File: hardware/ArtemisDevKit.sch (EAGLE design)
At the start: 77 parts, among them J1 USB, J10 SMD, J11 SMD, J12 PTH, J14 PTH, J2 CORTEX_JTAG_DEBUG_MINIMUM_PTH, J22 PTH, J23 PTH, J24 PTH, J25 PTH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

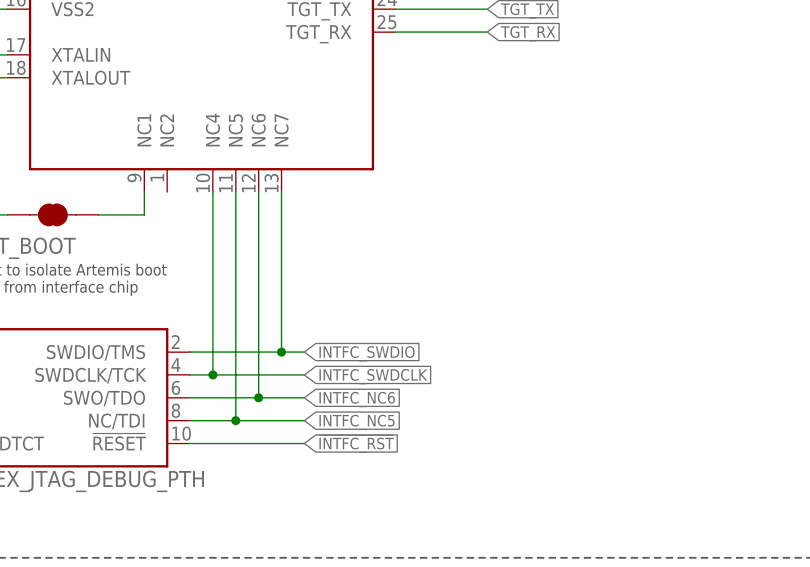
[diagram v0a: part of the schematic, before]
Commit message: add test points for interface JTAG
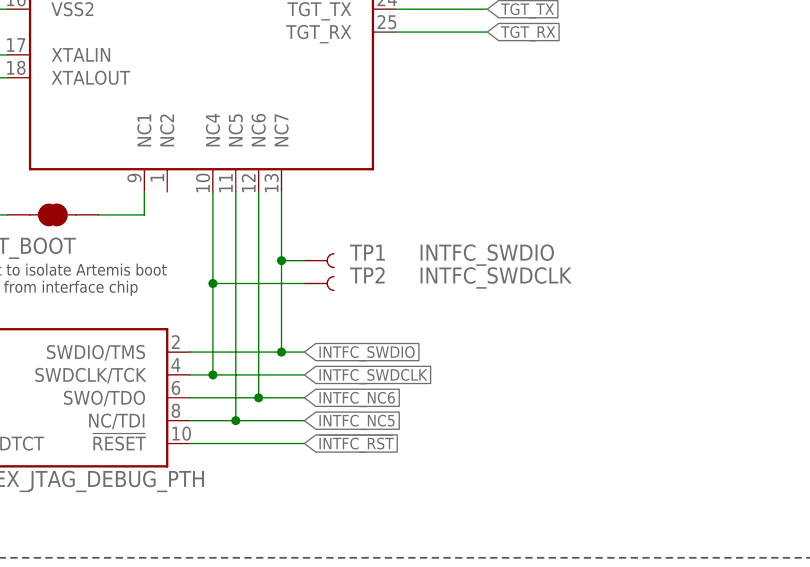
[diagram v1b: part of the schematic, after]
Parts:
- added TP1: INTFC_SWDIO, SparkFun-Connectors:TEST-POINT3
- added TP2: INTFC_SWDCLK, SparkFun-Connectors:TEST-POINT3
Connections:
- net INTFC_SWDCLK: now also TP2.1
- net INTFC_SWDIO: now also TP1.1
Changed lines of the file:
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@@
 <part name="U1" library="SparkFun-IC-Microcontroller" deviceset="DAPLINK_KL26Z128VFM4" device=""/>
 <part name="LOGO2" library="SparkFun-Aesthetics" deviceset="SFE_LOGO_NAME_FLAME" device=".2_INCH"/>
+<part name="TP1" library="SparkFun-Connectors" deviceset="TEST-POINT" device="3" value="INTFC_SWDIO"/>
+<part name="TP2" library="SparkFun-Connectors" deviceset="TEST-POINT" device="3" value="INTFC_SWDCLK"/>
 </parts>
 <sheets>
@@
 <instance part="U1" gate="G$1" x="88.9" y="187.96" smashed="yes"/>
 <instance part="LOGO2" gate="G$1" x="337.82" y="241.3" smashed="yes"/>
+<instance part="TP1" gate="G$1" x="101.6" y="144.78" smashed="yes">
+<attribute name="NAME" x="106.68" y="144.78" size="1.778" layer="95" font="vector"/>
+<attribute name="VALUE" x="114.3" y="144.78" size="1.778" layer="96" font="vector"/>
+</instance>
+<instance part="TP2" gate="G$1" x="101.6" y="142.24" smashed="yes">
+<attribute name="NAME" x="106.68" y="142.24" size="1.778" layer="95" font="vector"/>
+<attribute name="VALUE" x="114.3" y="142.24" size="1.778" layer="96" font="vector"/>
+</instance>
 </instances>
 <busses>
@@
 <label x="101.6" y="134.62" size="1.27" layer="95" font="vector" xref="yes"/>
 <wire x1="99.06" y1="134.62" x2="88.9" y2="134.62" width="0.1524" layer="91"/>
-<wire x1="99.06" y1="134.62" x2="99.06" y2="152.4" width="0.1524" layer="91"/>
+<wire x1="99.06" y1="134.62" x2="99.06" y2="144.78" width="0.1524" layer="91"/>
 <junction x="99.06" y="134.62"/>
 <pinref part="U1" gate="G$1" pin="NC7"/>
+<pinref part="TP1" gate="G$1" pin="1"/>
+<wire x1="99.06" y1="144.78" x2="99.06" y2="152.4" width="0.1524" layer="91"/>
+<wire x1="101.6" y1="144.78" x2="99.06" y2="144.78" width="0.1524" layer="91"/>
+<junction x="99.06" y="144.78"/>
 </segment>
 </net>
@@
 <label x="101.6" y="132.08" size="1.27" layer="95" font="vector" xref="yes"/>
 <wire x1="91.44" y1="132.08" x2="88.9" y2="132.08" width="0.1524" layer="91"/>
-<wire x1="91.44" y1="132.08" x2="91.44" y2="152.4" width="0.1524" layer="91"/>
+<wire x1="91.44" y1="132.08" x2="91.44" y2="142.24" width="0.1524" layer="91"/>
 <junction x="91.44" y="132.08"/>
 <pinref part="U1" gate="G$1" pin="NC4"/>
-</segment>
-</net>
+<pinref part="TP2" gate="G$1" pin="1"/>
+<wire x1="91.44" y1="142.24" x2="91.44" y2="152.4" width="0.1524" layer="91"/>
+<wire x1="101.6" y1="142.24" x2="91.44" y2="142.24" width="0.1524" layer="91"/>
+<junction x="91.44" y="142.24"/>
+</segment>
+</net>

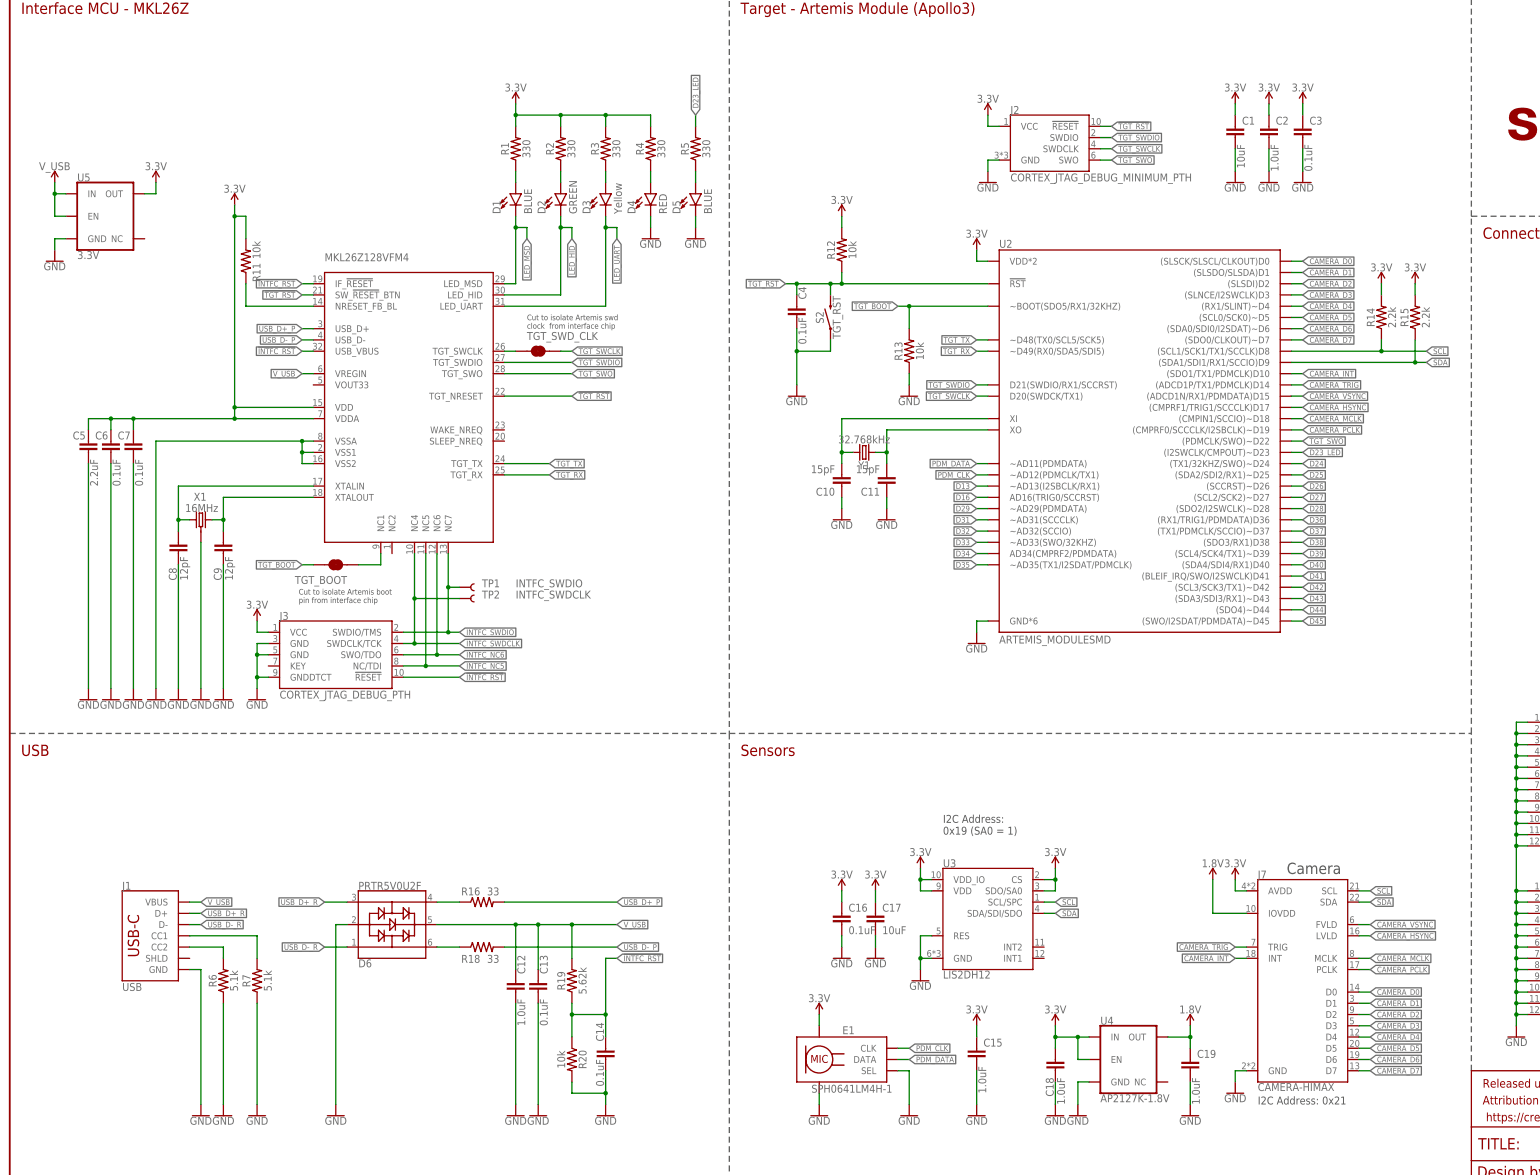
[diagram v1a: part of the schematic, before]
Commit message: fix camera connector
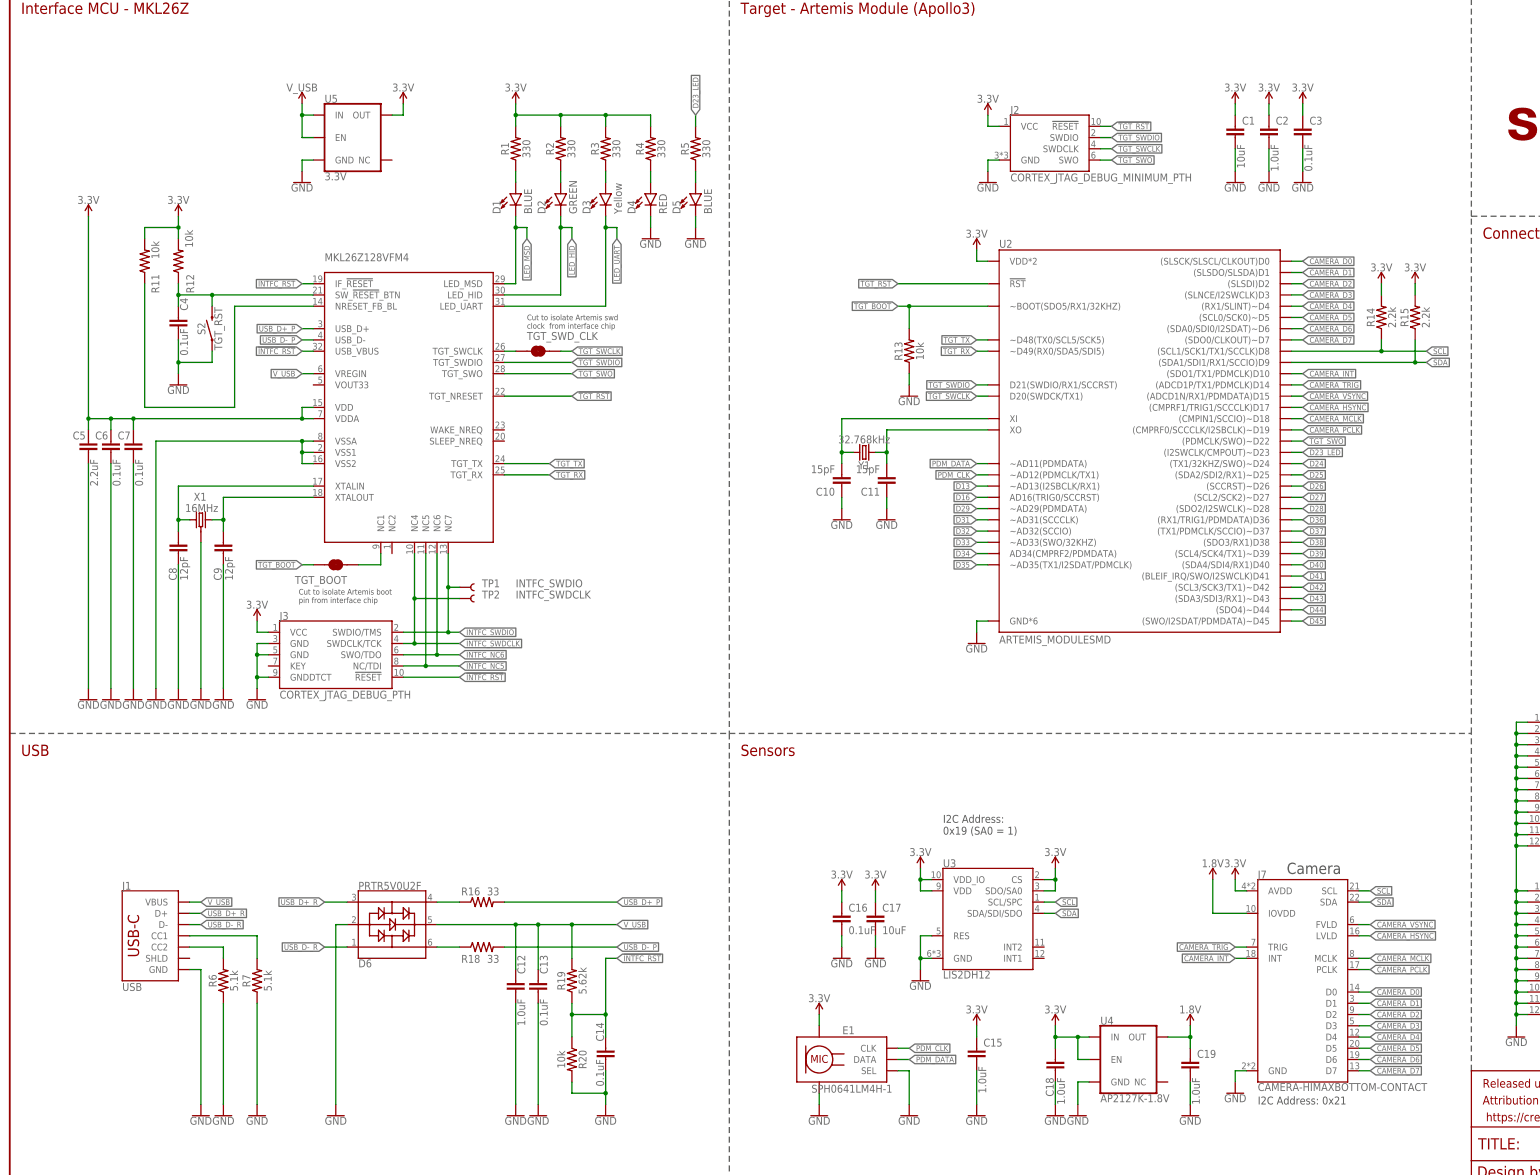
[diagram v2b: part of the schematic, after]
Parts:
- J7: value CAMERA-HIMAX -> CAMERA-HIMAXBOTTOM-CONTACT; device SparkFun-Connectors:CAMERA-HIMAX -> SparkFun-Connectors:CAMERA-HIMAXBOTTOM-CONTACT
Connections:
- new net !RST!_BTN: C4.1, R12.1, S2.2, U1.SW_!RESET!_BTN
- net !TGT_RST: no longer C4.1, R12.1, S2.2, U1.SW_!RESET!_BTN
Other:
- moved on the sheet: C4, R11, R12, S2, U5

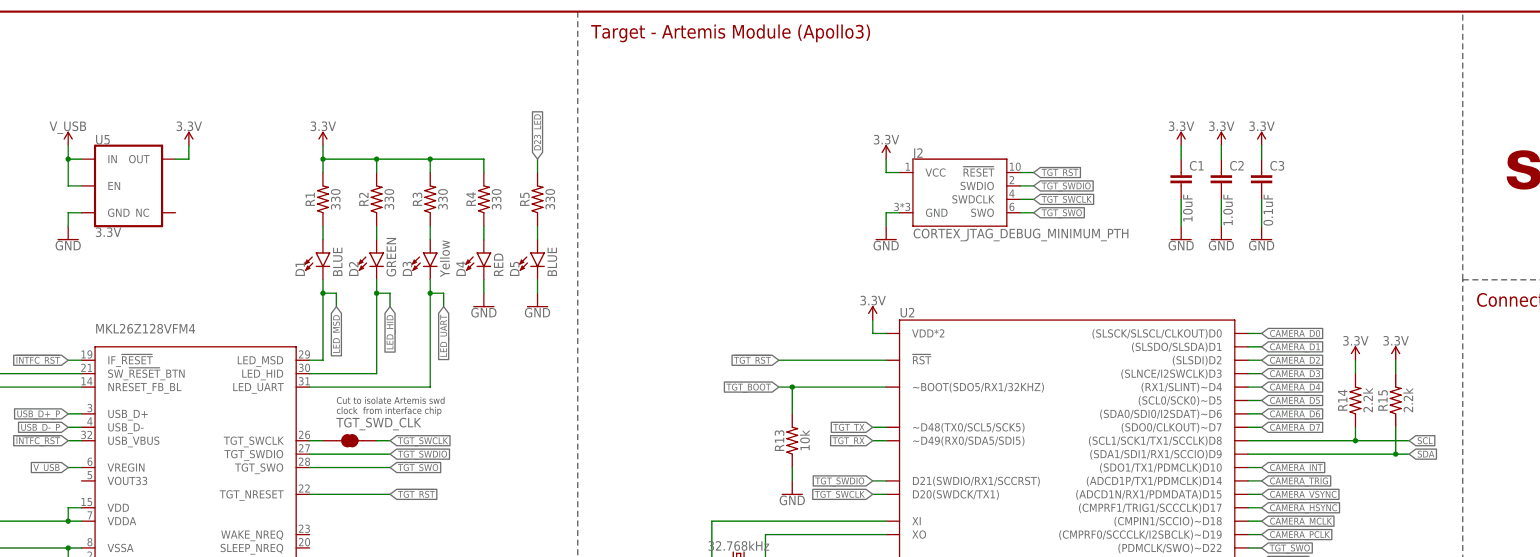
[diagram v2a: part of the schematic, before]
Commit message: final design checklist
-removed I2C PU resistors
- switched bubble labels to UPPER CASE
- ran checklist
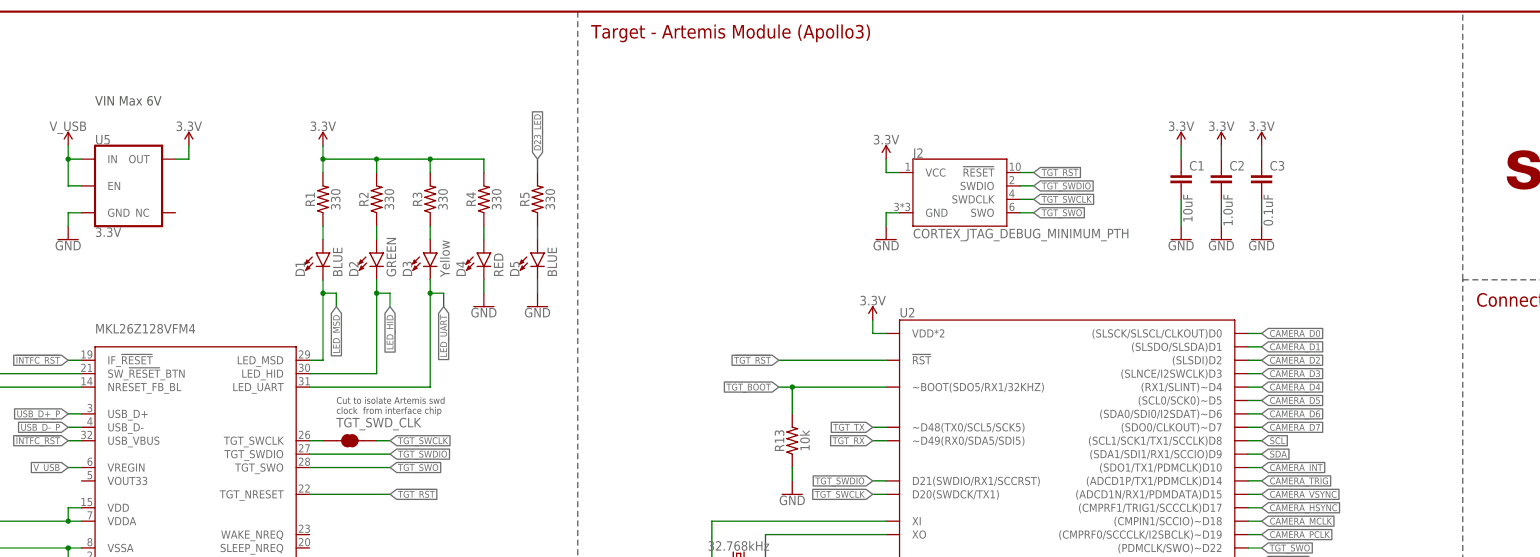
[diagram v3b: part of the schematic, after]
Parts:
- removed R14, R15: 2.2k, SparkFun-Resistors:2.2KOHM-0603-1/10W-1%
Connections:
- net 3.3V: no longer R14.2, R15.2
- net SCL: no longer R14.1
- net SDA: no longer R15.1
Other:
- note added: "VIN Max 6V"
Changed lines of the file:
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@@
 <part name="J6" library="SparkFun-Connectors" deviceset="QWIIC_CONNECTOR" device="JS-1MM" value="QWIIC_RIGHT_ANGLE"/>
 <part name="GND28" library="SparkFun-PowerSymbols" deviceset="GND" device=""/>
-<part name="R15" library="SparkFun-Resistors" deviceset="2.2KOHM" device="-0603-1/10W-1%" value="2.2k"/>
-<part name="R14" library="SparkFun-Resistors" deviceset="2.2KOHM" device="-0603-1/10W-1%" value="2.2k"/>
 <part name="R13" library="SparkFun-Resistors" deviceset="10KOHM" device="-0603-1/10W-1%" value="10k"/>
 <part name="SUPPLY24" library="SparkFun-PowerSymbols" deviceset="3.3V" device=""/>
@@
 <part name="GND23" library="SparkFun-PowerSymbols" deviceset="GND" device=""/>
 <part name="TGT_BOOT" library="SparkFun-Jumpers" deviceset="JUMPER-SMT_2_NC_TRACE" device="_SILK" package3d_urn="urn:adsk.eagle:package:39281/1"/>
-<part name="SUPPLY11" library="SparkFun-PowerSymbols" deviceset="3.3V" device=""/>
-<part name="SUPPLY12" library="SparkFun-PowerSymbols" deviceset="3.3V" device=""/>
 <part name="SUPPLY6" library="SparkFun-PowerSymbols" deviceset="3.3V" device=""/>
 <part name="SUPPLY17" library="SparkFun-PowerSymbols" deviceset="1.8V" device=""/>
@@
 clock  from interface chip</text>
 <text x="363.22" y="180.34" size="1.778" layer="97" font="vector">power rail intended for output only</text>
+<text x="71.12" y="261.62" size="1.778" layer="97">VIN Max 6V</text>
 </plain>
 <instances>
@@
 <attribute name="VALUE" x="375.92" y="190.246" size="1.778" layer="96" font="vector" align="top-center"/>
 </instance>
-<instance part="R15" gate="G$1" x="317.5" y="205.74" smashed="yes" rot="R90">
-<attribute name="NAME" x="315.976" y="205.74" size="1.778" layer="95" font="vector" rot="R90" align="bottom-center"/>
-<attribute name="VALUE" x="319.024" y="205.74" size="1.778" layer="96" font="vector" rot="R90" align="top-center"/>
-</instance>
-<instance part="R14" gate="G$1" x="309.88" y="205.74" smashed="yes" rot="R90">
-<attribute name="NAME" x="308.356" y="205.74" size="1.778" layer="95" font="vector" rot="R90" align="bottom-center"/>
-<attribute name="VALUE" x="311.404" y="205.74" size="1.778" layer="96" font="vector" rot="R90" align="top-center"/>
-</instance>
 <instance part="R13" gate="G$1" x="203.2" y="198.12" smashed="yes" rot="R90">
 <attribute name="NAME" x="201.676" y="198.12" size="1.778" layer="95" font="vector" rot="R90" align="bottom-center"/>
@@
 <instance part="TGT_BOOT" gate="G$1" x="73.66" y="149.86" smashed="yes" rot="R180">
 <attribute name="NAME" x="76.2" y="147.32" size="1.778" layer="95" font="vector" rot="R180"/>
-</instance>
-<instance part="SUPPLY11" gate="G$1" x="309.88" y="213.36" smashed="yes">
-<attribute name="VALUE" x="309.88" y="216.154" size="1.778" layer="96" font="vector" align="bottom-center"/>
-</instance>
-<instance part="SUPPLY12" gate="G$1" x="317.5" y="213.36" smashed="yes">
-<attribute name="VALUE" x="317.5" y="216.154" size="1.778" layer="96" font="vector" align="bottom-center"/>
 </instance>
 <instance part="SUPPLY6" gate="G$1" x="365.76" y="160.02" smashed="yes">
@@
 </segment>
 <segment>
-<pinref part="R14" gate="G$1" pin="2"/>
-<wire x1="309.88" y1="213.36" x2="309.88" y2="210.82" width="0.1524" layer="91"/>
-<pinref part="SUPPLY11" gate="G$1" pin="3.3V"/>
-</segment>
-<segment>
-<pinref part="R15" gate="G$1" pin="2"/>
-<wire x1="317.5" y1="213.36" x2="317.5" y2="210.82" width="0.1524" layer="91"/>
-<pinref part="SUPPLY12" gate="G$1" pin="3.3V"/>
-</segment>
-<segment>
 <wire x1="365.76" y1="147.32" x2="365.76" y2="149.86" width="0.1524" layer="91"/>
 <wire x1="365.76" y1="149.86" x2="365.76" y2="160.02" width="0.1524" layer="91"/>
@@
 </segment>
 <segment>
-<wire x1="320.04" y1="198.12" x2="309.88" y2="198.12" width="0.1524" layer="91"/>
-<label x="320.04" y="198.12" size="1.27" layer="95" font="vector" xref="yes"/>
-<pinref part="R14" gate="G$1" pin="1"/>
-<wire x1="309.88" y1="198.12" x2="289.56" y2="198.12" width="0.1524" layer="91"/>
-<wire x1="309.88" y1="200.66" x2="309.88" y2="198.12" width="0.1524" layer="91"/>
-<junction x="309.88" y="198.12"/>
+<label x="292.1" y="198.12" size="1.27" layer="95" font="vector" xref="yes"/>
+<wire x1="292.1" y1="198.12" x2="289.56" y2="198.12" width="0.1524" layer="91"/>
 <pinref part="U2" gate="U1" pin="(SCL1/SCK1/TX1/SCCLK)D8"/>
 </segment>
@@
 </segment>
 <segment>
-<wire x1="320.04" y1="195.58" x2="317.5" y2="195.58" width="0.1524" layer="91"/>
-<label x="320.04" y="195.58" size="1.27" layer="95" font="vector" xref="yes"/>
-<pinref part="R15" gate="G$1" pin="1"/>
-<wire x1="317.5" y1="195.58" x2="289.56" y2="195.58" width="0.1524" layer="91"/>
-<wire x1="317.5" y1="200.66" x2="317.5" y2="195.58" width="0.1524" layer="91"/>
-<junction x="317.5" y="195.58"/>
+<label x="292.1" y="195.58" size="1.27" layer="95" font="vector" xref="yes"/>
+<wire x1="292.1" y1="195.58" x2="289.56" y2="195.58" width="0.1524" layer="91"/>
 <pinref part="U2" gate="U1" pin="(SDA1/SDI1/RX1/SCCIO)D9"/>
 </segment>
